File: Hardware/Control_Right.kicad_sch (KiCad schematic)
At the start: 31 parts, among them J4 BAT, J5 TagConnect, J6 0.96_TFT_MODULE, Q3 AO3401A, Q4 AO3401A, SW3 MSK12C02, SW4 RESET, U3 TPS61040DBV, U4 XIAO-NRF52840-PLUS

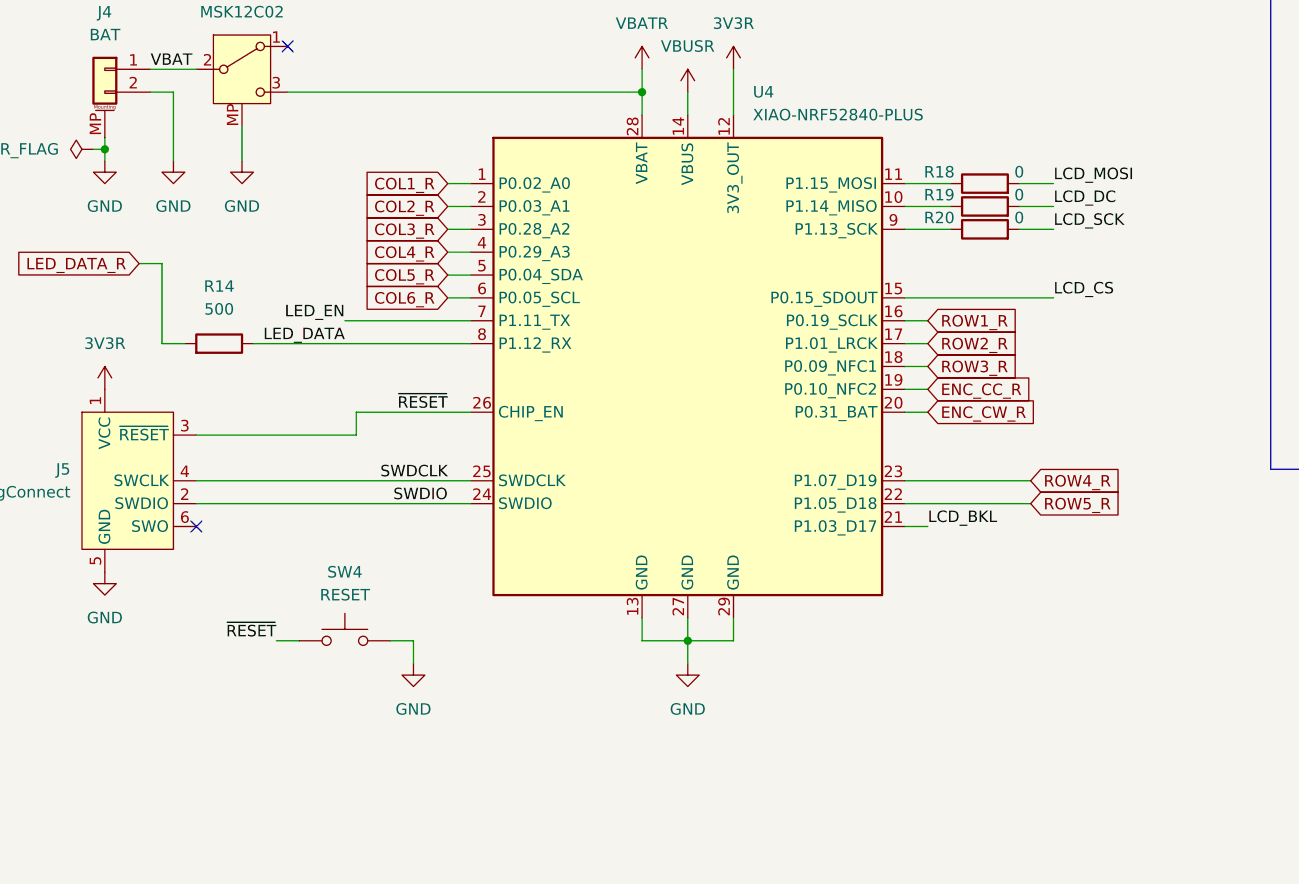
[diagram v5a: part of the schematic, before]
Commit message: Pinout and footprints
Updated the MCU footprints because the silkscreen was too close to the edge.
Updated the pinout for the MCUs. The left side seems to be ok, but the right side may need some adjustments.
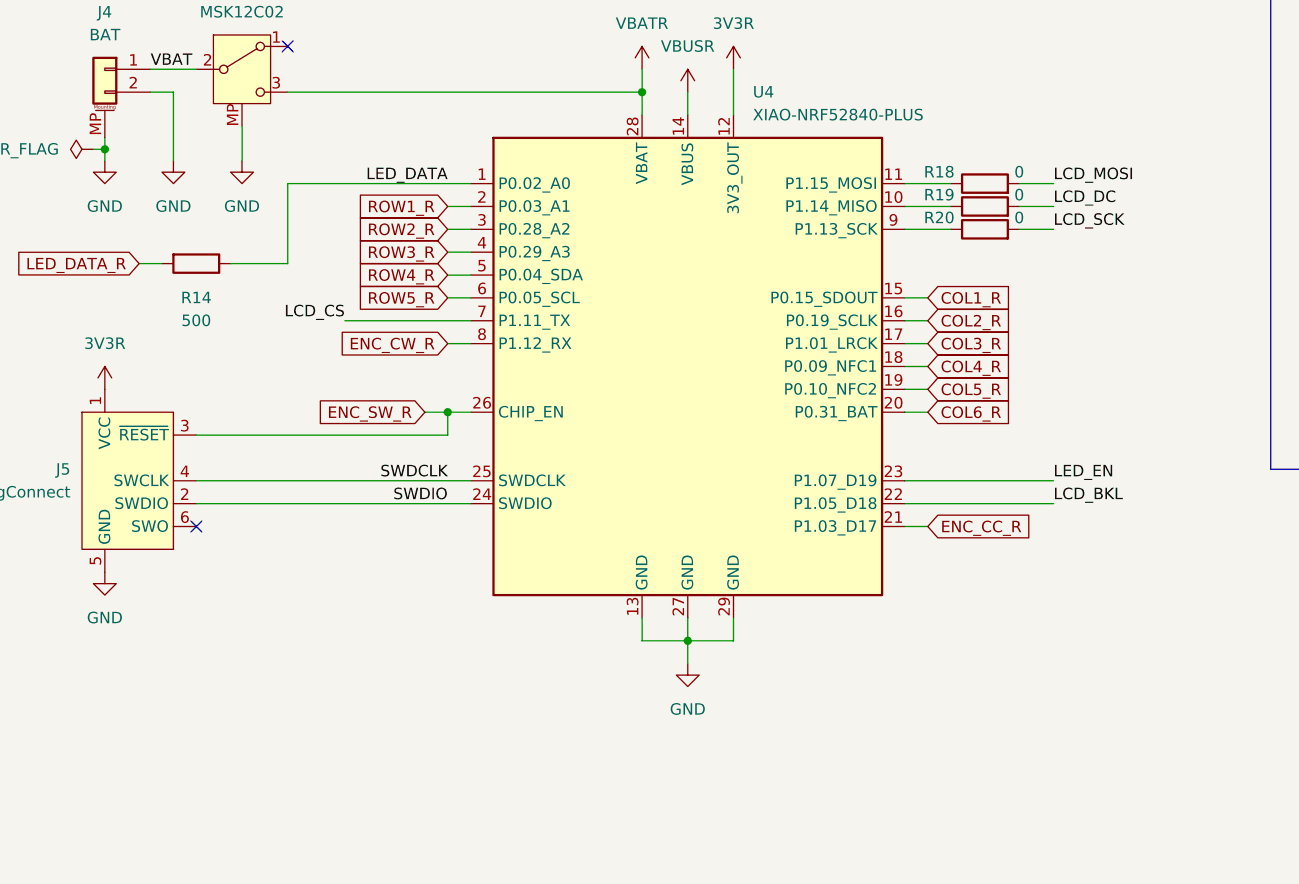
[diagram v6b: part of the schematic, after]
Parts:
- removed SW4: RESET, Button_Switch_SMD:SW_SPST_TS-1088-xR020, symbol Switch:SW_Push
- U4: footprint Custom_Parts:XIAO-NRF52840-PLUS-SMD -> Custom_Parts:XIAO-NRF52840-PLUS-SMD-EDGE
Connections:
- net COL1_R: now also U4.15 (P0.15_SDOUT); no longer U4.1 (P0.02_A0)
- net COL2_R: now also U4.16 (P0.19_SCLK); no longer U4.2 (P0.03_A1)
- net COL3_R: now also U4.17 (P1.01_LRCK); no longer U4.3 (P0.28_A2)
- net COL4_R: now also U4.18 (P0.09_NFC1); no longer U4.4 (P0.29_A3)
- net COL5_R: now also U4.19 (P0.10_NFC2); no longer U4.5 (P0.04_SDA)
- net COL6_R: now also U4.20 (P0.31_BAT); no longer U4.6 (P0.05_SCL)
- net ENC_CC_R: now also U4.21 (P1.03_D17); no longer U4.19 (P0.10_NFC2)
- net ENC_CW_R: now also U4.8 (P1.12_RX); no longer U4.20 (P0.31_BAT)
- net LCD_BKL: now also U4.22 (P1.05_D18); no longer U4.21 (P1.03_D17)
- net LCD_CS: now also U4.7 (P1.11_TX); no longer U4.15 (P0.15_SDOUT)
- net LED_DATA: now also U4.1 (P0.02_A0); no longer U4.8 (P1.12_RX)
- net LED_EN: now also U4.23 (P1.07_D19); no longer U4.7 (P1.11_TX)
- net ROW1_R: now also U4.2 (P0.03_A1); no longer U4.16 (P0.19_SCLK)
- net ROW2_R: now also U4.3 (P0.28_A2); no longer U4.17 (P1.01_LRCK)
- net ROW3_R: now also U4.4 (P0.29_A3); no longer U4.18 (P0.09_NFC1)
- net ROW4_R: now also U4.5 (P0.04_SDA); no longer U4.23 (P1.07_D19)
- net ROW5_R: now also U4.6 (P0.05_SCL); no longer U4.22 (P1.05_D18)
- net ~{RESET} renamed ENC_SW_R
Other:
- moved on the sheet: R14

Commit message: Reset button and LED switch
Added an LED power switch.
Returned the reset button for bootloader access.
Focus on changing the display to an e-ink one for lower power consumption.
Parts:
- removed R13: 100K, Resistor_SMD:R_0603_1608Metric, symbol Device:R
- removed R16: 470K, Resistor_SMD:R_0603_1608Metric, symbol Device:R
- removed R17: 150K, Resistor_SMD:R_0603_1608Metric, symbol Device:R
- removed U3: TPS61040DBV, Package_TO_SOT_SMD:SOT-23-5, symbol Regulator_Switching:TPS61040DBV
- added R12: 100K, Resistor_SMD:R_0603_1608Metric, symbol Device:R
- added R14: 470K, Resistor_SMD:R_0603_1608Metric, symbol Device:R
- added SW5: SW_Push, Button_Switch_SMD:SW_SPST_TS-1088-xR020, symbol Switch:SW_Push
- added SW6: MSK12C02, Custom_Parts:MSK12C02, symbol Custom_Parts:MSK12C02
- added U4: TPS61040DBV, Package_TO_SOT_SMD:SOT-23-5, symbol Regulator_Switching:TPS61040DBV
- R15: value 10K -> 150K; JLC Part 0603WAF1002T5E -> C22807; Manufacturer Part 0603WAF1002T5E -> 0603WAF1503T5E
- renumbered R14 to R13, R18 to R16, R19 to R17, R20 to R18, R21 to R19, R22 to R20, R23 to R21, R24 to R22, SW3 to SW4, U4 to U3
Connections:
- net 5VR: now also R14.1
- net ENC_SW_R: now also U3.23 (P1.07_D19); no longer J5.3 (~{RESET}), U3.26 (CHIP_EN)
- net GND: now also R15.2, R12.2, SW5.2, SW6.MP, U4.2 (GND); no longer R15.1
- net VBUSR: now also R12.1
- net VFB: now also R15.1, R14.2, U4.3 (FB)
- net VREGR: now also SW6.3 (C), U4.4 (EN), U4.5 (VIN); no longer D4.1 (K), Q3.2 (S)
- net VSW: now also U4.1 (SW)
- removed net LED_EN: R15.2, U3.23 (P1.07_D19)
- new net VCOM: D4.1 (K), Q3.2 (S), SW6.2 (B)
- new net ~{RESET}: J5.3 (~{RESET}), SW5.1, U3.26 (CHIP_EN)
- no-connect marks 2 -> 3
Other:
- moved on the sheet: C11, C12, D6, J4, J5, J6, Q4, R13, R16, R17, R18, R19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

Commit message: MIP display and LED enable
Return of the LED enable via GPIO.
Changed the TFT display for a MPI panel. It's more expensive than an e-ink one, but the sharpness is really nice.
Need to remove the numbers row to go for a true Corne-ish layout.
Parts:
- removed C7: 1u, Capacitor_SMD:C_0603_1608Metric, symbol Device:C
- removed D5, D6: DSK24, Diode_SMD:D_SOD-123F, symbol Device:D_Schottky
- removed J6: 0.96_TFT_MODULE, Custom_Parts:0.96_TFT_MODULE, symbol Custom_Parts:0.96_TFT_MODULE
- removed Q3, Q4: AO3401A, Package_TO_SOT_SMD:SOT-23, symbol Transistor_FET:AO3401A
- removed R14: 470K, Resistor_SMD:R_0603_1608Metric, symbol Device:R
- removed R15: 150K, Resistor_SMD:R_0603_1608Metric, symbol Device:R
- removed R19: 100, Resistor_SMD:R_0603_1608Metric, symbol Device:R
- removed R20, R21: 10K, Resistor_SMD:R_0603_1608Metric, symbol Device:R
- removed R22: 22, Resistor_SMD:R_0603_1608Metric, symbol Device:R
- removed SW6: MSK12C02, Custom_Parts:MSK12C02, symbol Custom_Parts:MSK12C02
- removed U4: TPS61040DBV, Package_TO_SOT_SMD:SOT-23-5, symbol Regulator_Switching:TPS61040DBV
- added C13: 1n, Capacitor_SMD:C_0603_1608Metric, symbol Device:C
- added C14: 1u, Capacitor_SMD:C_0603_1608Metric, symbol Device:C
- added D3: DSK24, Diode_SMD:D_SOD-123F, symbol Device:D_Schottky
- added FB3, FB4: 600, Inductor_SMD:L_0603_1608Metric, symbol Device:FerriteBead
- added J6: 1.08_MIP_MODULE, Custom_Parts:1.08_MIP_MODULE, symbol Custom_Parts:1.08_MIP_MODULE
- added Q2: AO3401A, Package_TO_SOT_SMD:SOT-23, symbol Transistor_FET:AO3401A
- added R10: 100K, Resistor_SMD:R_0603_1608Metric, symbol Device:R
- added R11: 10K, Resistor_SMD:R_0603_1608Metric, symbol Device:R
- added R13: 150K, Resistor_SMD:R_0603_1608Metric, symbol Device:R
- added U3: TPS61040DBV, Package_TO_SOT_SMD:SOT-23-5, symbol Regulator_Switching:TPS61040DBV
- C10: value 4.7u -> 10p; footprint Capacitor_SMD:C_1206_3216Metric -> Capacitor_SMD:C_0603_1608Metric; JLC Part C29823 -> C1634; Manufacturer Part 1206B475K500NT -> CL10C100JB8NNNC
- C11: value 1u -> 4.7u; footprint Capacitor_SMD:C_0603_1608Metric -> Capacitor_SMD:C_1206_3216Metric; JLC Part C15849 -> C29823; Manufacturer Part CL10A105KB8NNNC -> 1206B475K500NT
- C8: value 4.7u -> 1u; footprint Capacitor_SMD:C_1206_3216Metric -> Capacitor_SMD:C_0603_1608Metric; JLC Part C29823 -> C15849; Manufacturer Part 1206B475K500NT -> CL10A105KB8NNNC
- C9: value 10p -> 4.7u; footprint Capacitor_SMD:C_0603_1608Metric -> Capacitor_SMD:C_1206_3216Metric; JLC Part C1634 -> C29823; Manufacturer Part CL10C100JB8NNNC -> 1206B475K500NT
- R12: value 100K -> 470K; JLC Part C25803 -> C23178; Manufacturer Part 0603WAF1003T5E -> 0603WAF4703T5E
- renumbered R16 to R14, R17 to R15, R18 to R16, R13 to R9, SW4 to SW3, SW5 to SW4, U3 to U4
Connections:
- net LCD_RES is gone; now on net 5VR: C11.1
- net VCOM is gone; now on net 5VR: D4.1 (K)
- net 3V3R: now also C14.1, FB3.1, J6.7 (VDD); no longer C12.1
- net 5VR: now also R12.1; no longer C9.1
- net GND: now also C9.2, C13.2, C14.2, FB4.1, J6.4 (EXTCOM), J6.8 (EXTMOD), J6.9 (VSS), J6.MP, R10.2, R11.1, R13.2, U3.2 (GND); no longer C10.2, C12.2, R12.2
- net VBATR: now also Q2.3 (D)
- net VBUSR: now also C8.1, D3.2 (A), Q2.1 (G), R10.1; no longer D4.2 (A), R12.1
- net VFB: now also C10.2, R12.2, R13.1, U3.3 (FB); no longer C9.2
- net VREGR: now also C9.1, D3.1 (K), Q2.2 (S), U3.5 (VIN); no longer C8.1
- net VSW: now also D4.2 (A), U3.1 (SW)
- net LCD_BKL renamed MIP_EN
- net MIP_EN: now also C13.1, J6.5 (DISP)
- net LCD_CS renamed LED_EN
- net LED_EN: now also R11.2, U3.4 (EN)
- net LCD_DC renamed MIP_CS
- net MIP_CS: now also J6.3 (SCS)
- net LCD_MOSI renamed MIP_MOSI
- net MIP_MOSI: now also J6.2 (SI)
- net LCD_SCK renamed MIP_SCK
- net MIP_SCK: now also J6.1 (SCLK)
- new net MIP_VDDA: C12.1, FB3.2, J6.6 (VDDA)
- new net MIP_VSSA: C12.2, FB4.2, J6.10 (VSSA)
- no-connect marks 3 -> 2
